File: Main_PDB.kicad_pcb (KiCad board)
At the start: 4 copper layers, 175.5 x 85.5 mm, 134 parts, among them Q4 NMOS, Q5 NMOS, Q6 NMOS, Q7 NMOS, Q8 NMOS, U10 ACS758LCB-100U-PFF-T, U11 ACS758LCB-100U-PFF-T, U12 ACS758LCB-100U-PFF-T, U2 LM5148RGYR, U3 LMR36015ARNXR, U4 ACS758LCB-100U-PFF-T, U5 ACS758LCB-100U-PFF-T, U6 UCC27511DBVR, U8 ACS758LCB-100U-PFF-T, U9 ACS758LCB-100U-PFF-T

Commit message: begun placement for 12V buck
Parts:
- added F2: ~, LITTLEFUSE_178.6165.0002:LITTELFUSE_178.6165.0002, F.Cu at (414.4, 238.1)
- added F3: ~, LITTLEFUSE_178.6165.0002:LITTELFUSE_178.6165.0002, F.Cu at (192.4, 46.4)
- added F4: ~, LITTLEFUSE_178.6165.0002:LITTELFUSE_178.6165.0002, F.Cu at (192.4, 54.0)
- added F5: ~, LITTLEFUSE_178.6165.0002:LITTELFUSE_178.6165.0002, F.Cu at (192.4, 61.5)
- added F6: ~, LITTLEFUSE_178.6165.0002:LITTELFUSE_178.6165.0002, F.Cu at (192.4, 69.1)
- added F7: ~, LITTLEFUSE_178.6165.0002:LITTELFUSE_178.6165.0002, F.Cu at (192.4, 76.6)
- moved D3 454.0 mm to (423.5, 297.9)
- moved CCSF1 452.1 mm to (428.3, 321.1)
- moved RCSF1 447.2 mm to (421.5, 325.6)
- moved CCS1 446.9 mm to (427.4, 314.1)
- moved CBULK1 407.8 mm to (415.2, 310.5)
- moved RSEN1 398.8 mm to (436.6, 249.4)
- moved CIN5B1 394.1 mm to (413.1, 270.4)
- moved L2 385.0 mm to (426.7, 254.1)
- moved U5 380.1 mm to (447.9, 307.2), turned to 90 degrees
- moved Q5 379.7 mm to (429.5, 263.6)
- moved Q4 376.7 mm to (422.7, 263.6)
- moved CBOOT1 375.1 mm to (373.1, 254.5)
- moved CHF1 371.2 mm to (373.1, 260.8)
- moved CCOMP1 368.9 mm to (366.4, 260.5)
- moved CVDDA1 364.9 mm to (366.4, 266.4)
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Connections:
- D10 pad 1: +48V-B -> +48V_BATT
- RESTOP3 pad 1: +48V-B -> +48V_BATT

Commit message: 12V buck layout progressed
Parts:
- moved RCON1 80.1 mm to (447.4, 257.0), turned to -90 degrees
- moved RSF1 79.2 mm to (445.9, 257.0), turned to -90 degrees
- moved RCOMP1 78.1 mm to (445.2, 259.3), turned to 180 degrees
- moved CCOMP1 78.1 mm to (444.4, 257.0), turned to 90 degrees
- moved CVDDA1 75.1 mm to (441.1, 258.6), turned to -90 degrees
- moved RFBS1 74.5 mm to (448.0, 260.7), turned to 90 degrees
- moved CHF1 69.9 mm to (442.9, 258.6), turned to 90 degrees
- moved CBOOT1 66.8 mm to (438.9, 265.6), turned to 180 degrees
- moved CVCC1 66.1 mm to (439.3, 258.4), turned to 90 degrees
- moved CIN5B1 26.0 mm to (437.1, 260.4), turned to -90 degrees
- moved U2 5.38 mm to (441.9, 262.5)
- moved CIN4B1 1.82 mm to (410.7, 261.1)
- moved CIN2B1 1.82 mm to (410.7, 267.8)
- moved CIN3B1 1.82 mm to (410.7, 264.4)
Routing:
- net Net-(U2-VDDA): track 0.00 -> 8.62 mm, vias 0 -> 2
- net Net-(U2-FB): track 0.00 -> 6.48 mm, vias 0 -> 2
- net Net-(U2-CNFG): track 0.00 -> 5.11 mm, vias 0 -> 2
- net Net-(U2-RT): track 0.00 -> 4.18 mm, vias 0 -> 2
- net AGND: track 42.6 -> 45.6 mm
- net Net-(U2-VCC): track 0.00 -> 2.35 mm
- net /12V_NMOS: track 0.00 -> 2.17 mm
- net Net-(U2-CBOOT): track 0.00 -> 1.65 mm
- net Net-(U2-EXTCOMP): track 0.00 -> 1.51 mm
- net Net-(Q5-G): track 0.00 -> 0.15 mm, vias 0 -> 1
- net Net-(Q4-G): vias 0 -> 2
- added copper zone on F.Cu, net /12V_FUSE
- added copper zone on F.Cu, net /12V_NMOS

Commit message: 12V layout progress
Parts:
- moved RFBS1 24.0 mm to (431.7, 278.4), turned to 0 degrees
- moved RCON1 24.0 mm to (435.4, 277.8), turned to 180 degrees
- moved RSF1 21.9 mm to (435.4, 276.3), turned to 180 degrees
- moved RCOMP1 20.2 mm to (433.1, 275.6), turned to 90 degrees
- moved CCOMP1 19.9 mm to (435.4, 274.8), turned to 0 degrees
- moved COUT4B1 18.3 mm to (440.7, 262.3), turned to 0 degrees
- moved CHF1 17.3 mm to (433.9, 273.3), turned to 0 degrees
- moved U2 15.5 mm to (430.0, 272.4), turned to 180 degrees
- moved COUT3B1 15.3 mm to (441.3, 259.7), turned to 0 degrees
- moved CVDDA1 14.8 mm to (433.9, 271.5), turned to 180 degrees
- moved CBOOT1 12.6 mm to (426.9, 269.3), turned to 90 degrees
- moved CVCC1 12.5 mm to (434.1, 269.7), turned to 0 degrees
- moved COUT2B1 11.5 mm to (441.3, 256.4), turned to 0 degrees
- moved CIN5B1 8.70 mm to (432.0, 267.5), turned to 180 degrees
- moved COUT1B1 8.39 mm to (441.2, 253.1), turned to 0 degrees
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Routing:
- net /12V_IND: track 0.00 -> 27.2 mm, vias 0 -> 2

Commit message: PCB updates
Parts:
- added J5: 24V Out -> Jetson, Connector_Phoenix_MC:PhoenixContact_MC_1,5_2-G-3.81_1x02_P3.81mm_Horizontal, F.Cu at (114.2, 25.9)
- added J6: 24V Out -> USB-C-PD controller, Connector_Phoenix_MC:PhoenixContact_MC_1,5_2-G-3.81_1x02_P3.81mm_Horizontal, F.Cu at (125.4, 25.9)
- added RDIV1: 1M, Resistor_SMD:R_0603_1608Metric, F.Cu at (108.5, 24.0)
- added RDIV2: 24.9k, Resistor_SMD:R_0603_1608Metric, F.Cu at (108.5, 26.5)
- added RFB1A2: 291k, Resistor_SMD:R_0603_1608Metric, F.Cu at (108.5, 29.0)
- added RFB2B2: 10k, Resistor_SMD:R_0603_1608Metric, F.Cu at (108.5, 31.5)
- added RFBC1: 1.65M, Resistor_SMD:R_0603_1608Metric, F.Cu at (108.5, 34.0)
- added RPU1: 10K, Resistor_SMD:R_0603_1608Metric, F.Cu at (108.5, 36.5)
- added U1: TLV3011AIDBVT, Footprints:SOT95P280X145-6N, F.Cu at (113.7, 37.1)
- L2: value 3.8uH -> 10uH; footprint Footprints:MSS1038183MLC -> Inductor_SMD:L_Coilcraft_XAL8080-XXX
- L3: value 3.8uH -> 4.7uH; footprint Footprints:MSS1038183MLC -> Inductor_SMD:L_Coilcraft_XAL8080-XXX
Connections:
- net /Back_curr_sing renamed Net-(U1-OUT)
- CBULK1 pad 1: +12V -> +24V
- CCS3 pad 1: +12V -> +6V
- D3 pad 1: +12V -> +24V
- U5 pad 5: +12V -> +24V
- U5 pad 5_1: +12V -> +24V
- U5 pad 5_10: +12V -> +24V
- U5 pad 5_11: +12V -> +24V
- U5 pad 5_12: +12V -> +24V
- U5 pad 5_13: +12V -> +24V
- U5 pad 5_14: +12V -> +24V
- U5 pad 5_15: +12V -> +24V
- U5 pad 5_16: +12V -> +24V
- U5 pad 5_2: +12V -> +24V
- U5 pad 5_3: +12V -> +24V
- U5 pad 5_4: +12V -> +24V
- U5 pad 5_5: +12V -> +24V
- U5 pad 5_6: +12V -> +24V
- U5 pad 5_7: +12V -> +24V
- U5 pad 5_8: +12V -> +24V
- U5 pad 5_9: +12V -> +24V
- U6 pad 1: +12V -> +6V

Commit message: ESTOP curr sen PCB layout
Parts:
- added JESTOP1: ESTOP_IN, MountingHole:MountingHole_5.3mm_M5_Pad, F.Cu at (503.2, 118.5)
- added JESTOP2: ESTOP_OUT, MountingHole:MountingHole_5.3mm_M5_Pad, F.Cu at (503.2, 134.8)
- moved U8 422.5 mm to (477.6, 140.2), turned to -90 degrees
- moved CCS4 397.2 mm to (464.0, 138.2)
- moved CCSF4 394.8 mm to (462.8, 141.0), turned to -90 degrees
- moved RCSF4 390.0 mm to (463.6, 143.6), turned to 180 degrees
- moved CBOOT1 198.7 mm to (228.5, 258.8)
- moved CHF1 198.7 mm to (235.5, 262.8)
- moved CIN2B1 198.7 mm to (212.3, 257.2)
- moved CIN3B1 198.7 mm to (212.3, 253.9)
- moved CIN4B1 198.7 mm to (212.3, 250.6)
- moved COUT1B1 198.7 mm to (242.8, 242.6)
- moved COUT2B1 198.7 mm to (242.9, 245.9)
- moved COUT3B1 198.7 mm to (242.9, 249.2)
- moved CVCC1 198.7 mm to (235.7, 259.2)
- moved F2 198.7 mm to (211.2, 232.8)
- moved L2 198.7 mm to (228.3, 243.6)
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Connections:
- D10 pad 1: +48V_BATT -> /48V_FUSE
- RESTOP3 pad 1: +48V_BATT -> /48V_FUSE
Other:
- board size 175.5 x 85.5 mm -> 175.5 x 162.7 mm

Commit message: Added actuator connector footprints
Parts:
- added J10: Conn_01x02_MountingPin, Connector_AMASS:AMASS_XT30UPB-F_1x02_P5.0mm_Vertical, F.Cu at (450.0, 181.9)
- added J7: Conn_01x02_MountingPin, Connector_AMASS:AMASS_XT30UPB-F_1x02_P5.0mm_Vertical, F.Cu at (450.0, 160.2)
- added J8: Conn_01x02_MountingPin, Connector_AMASS:AMASS_XT30UPB-F_1x02_P5.0mm_Vertical, F.Cu at (450.0, 167.4)
- added J9: Conn_01x02_MountingPin, Connector_AMASS:AMASS_XT30UPB-F_1x02_P5.0mm_Vertical, F.Cu at (450.0, 174.7)
- moved U10 348.1 mm to (446.9, 207.6)
- moved U12 348.1 mm to (496.9, 207.9)
- moved U9 348.1 mm to (425.3, 207.6)
- moved U11 348.1 mm to (468.4, 207.6)
- moved CCSF4 48.3 mm to (498.8, 173.2), turned to 0 degrees
- moved RCSF4 47.5 mm to (501.4, 172.4), turned to -90 degrees
- moved CCS4 46.5 mm to (496.0, 172.0), turned to 90 degrees
- moved U8 27.3 mm to (498.0, 158.4), turned to 0 degrees
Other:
- board size 175.5 x 162.7 mm -> 175.5 x 234.8 mm

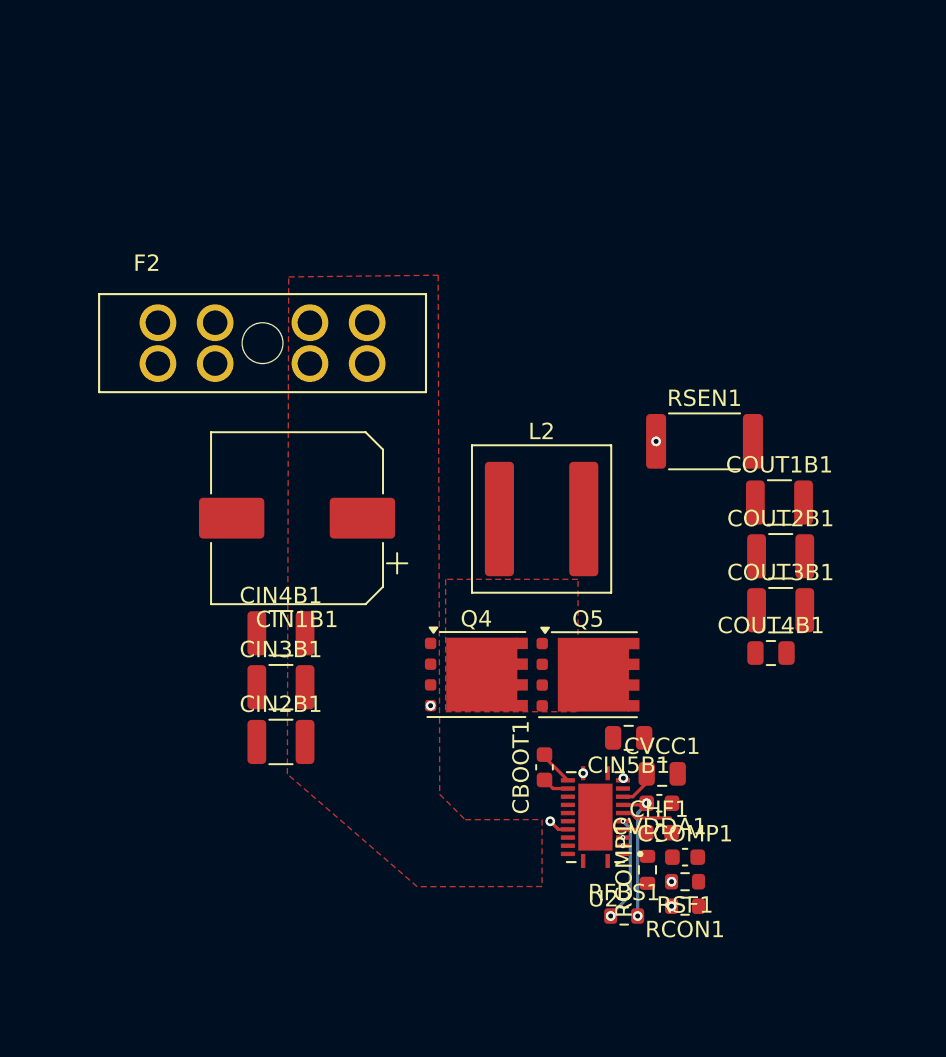
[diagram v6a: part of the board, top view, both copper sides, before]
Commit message: 12V buck almost finished
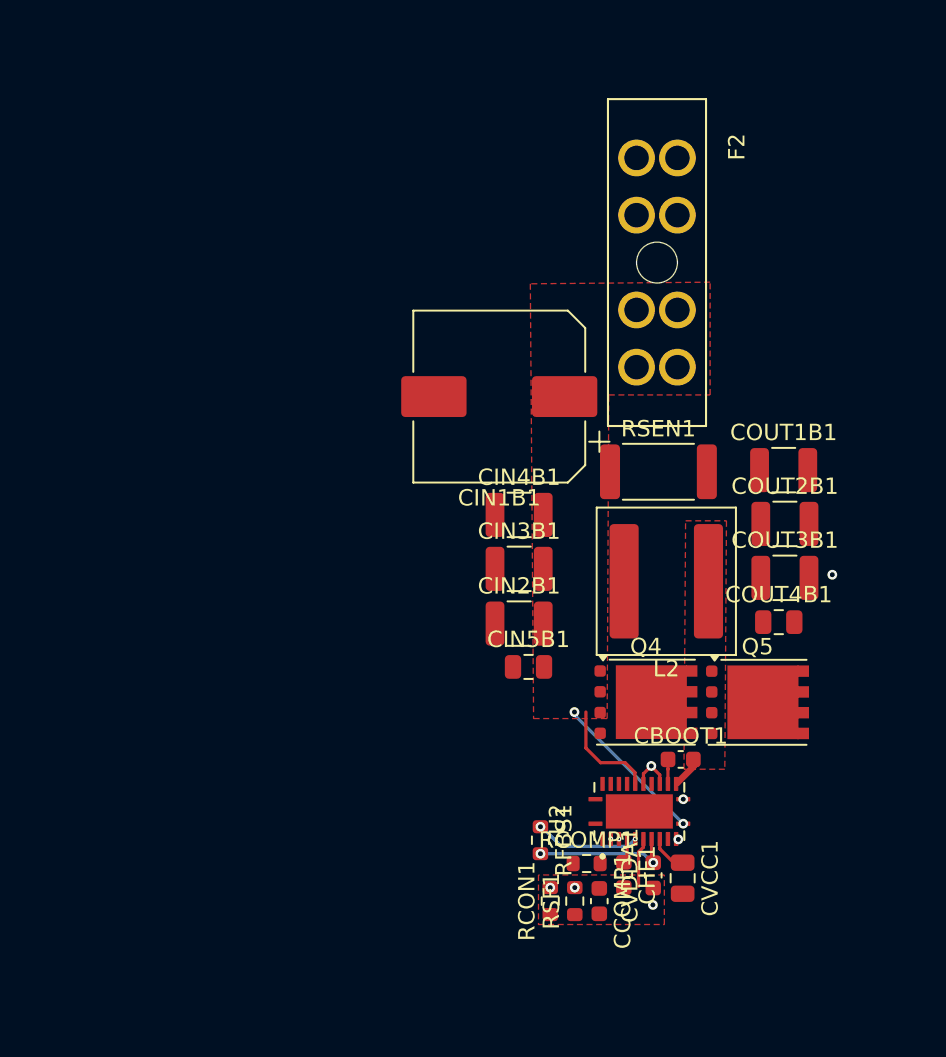
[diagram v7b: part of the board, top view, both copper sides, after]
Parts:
- moved F2 24.6 mm to (235.3, 227.9), turned to -90 degrees
- moved CIN2B1 16.3 mm to (226.9, 250.0)
- moved CIN3B1 16.3 mm to (226.9, 246.6)
- moved CIN4B1 16.3 mm to (226.9, 243.3)
- moved CIN1B1 14.4 mm to (225.7, 236.1)
- moved Q4 10.5 mm to (234.7, 254.8)
- moved Q5 10.5 mm to (241.5, 254.8)
- moved L2 8.53 mm to (235.9, 247.4), turned to 180 degrees
- moved CBOOT1 8.35 mm to (236.8, 258.3), turned to 0 degrees
- moved RCON1 8.25 mm to (228.8, 267.0), turned to 90 degrees
- moved CIN5B1 7.51 mm to (227.5, 252.6), turned to 0 degrees
- moved RFBS1 6.91 mm to (228.2, 263.2), turned to -90 degrees
- moved RSF1 6.85 mm to (230.3, 267.0), turned to 90 degrees
- moved CVCC1 6.51 mm to (236.9, 265.6), turned to -90 degrees
- moved CCOMP1 5.90 mm to (231.8, 267.0), turned to -90 degrees
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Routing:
- net /12V_IND: track 27.2 -> 0.00 mm, vias 2 -> 0
- net /12V_FUSE: track 0.00 -> 16.1 mm, vias 0 -> 2
- net AGND: track 45.6 -> 57.3 mm, vias 1 -> 3
- net PGND: vias 40 -> 41
- net Net-(Q4-G): vias 2 -> 1
- added copper zone on F.Cu, net (none)

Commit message: Buck draft done
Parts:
- moved RFB1A2 260.4 mm to (228.2, 260.2), turned to 90 degrees
- moved RFB2B2 260.1 mm to (226.7, 263.2), turned to 90 degrees
- moved RCSF1 84.5 mm to (275.3, 248.6)
- moved CCSF1 75.3 mm to (275.3, 250.5)
- moved CCS1 69.0 mm to (275.3, 252.4)
- moved CBULK1 53.6 mm to (258.7, 266.5)
- moved U5 47.9 mm to (262.1, 250.5)
- moved D3 34.6 mm to (257.9, 276.2)
- moved COUT4B1 14.0 mm to (250.2, 238.1), turned to 90 degrees
- moved COUT3B1 10.5 mm to (247.5, 237.7), turned to 90 degrees
- moved COUT2B1 6.30 mm to (244.2, 237.7), turned to 90 degrees
- moved COUT1B1 3.59 mm to (240.9, 237.8), turned to 90 degrees
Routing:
- net /12V_SEN: track 0.00 -> 23.9 mm, vias 0 -> 2
- net Net-(Q5-G): track 0.15 -> 8.09 mm, vias 1 -> 0
- net Net-(Q4-G): track 0.00 -> 7.42 mm, vias 1 -> 2
- net Net-(U2-EXTCOMP): track 1.51 -> 4.65 mm, vias 0 -> 2
- net Net-(U2-FB): track 6.48 -> 9.41 mm
- net /Com_cur: track 0.00 -> 1.92 mm
- net AGND: track 57.3 -> 59.1 mm
- net +3.3V: track 93.9 -> 95.7 mm
- net Net-(U5-VIOUT): track 0.00 -> 1.73 mm
- net Net-(CCOMP1-Pad1): track 0.00 -> 1.55 mm
- net /12V_FUSE: track 16.1 -> 17.6 mm
- net Net-(U2-VCC): track 2.35 -> 2.87 mm
- net PGND: vias 41 -> 66
- net /12V_NMOS: vias 0 -> 16
- added copper zone on F.Cu, net +24V
- added copper zone on F.Cu, net /12V_SEN
